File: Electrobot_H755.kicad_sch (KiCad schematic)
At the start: 107 parts, among them J1 Conn_XT30M, J10 Conn_01x04, J11 Conn_01x04, J12 Conn_01x04, J13 Conn_01x04, J14 Conn_01x04, J15 Conn_01x03, J16 Conn_01x03, J17 Conn_01x04, J18 Conn_01x03, J19 Conn_01x03, J2 Conn_01x04, J20 Conn_01x03, J21 Conn_01x03, J22 Conn_01x04, J23 Conn_01x03, J24 Conn_01x03, J25 Conn_01x03, J26 Conn_01x03, J27 Conn_01x02, J28 Conn_01x02, J29 Conn_01x02, J3 Conn_01x04, J30 Conn_01x02, J31 Conn_01x03, J32 Conn_01x03, J33 Conn_01x06, J34 Conn_01x06, J35 Conn_01x04, J36 Conn_01x02, J4 Conn_01x04, J5 Conn_01x04, J6 Conn_01x04, J7 Conn_01x04, J8 Conn_01x04, J9 Conn_01x04, U2 TSR_2-2450, U3 TSR_2-2465, U4 TSR_2-2465

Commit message: Correction empreinte condensateur
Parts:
- C4: footprint Capacitor_THT:C_Radial_D8.0mm_H11.5mm_P3.50mm -> Passive:C_Radial_D8.0mm_H11.5mm_P3.50mm
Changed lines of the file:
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@@
 			)
 		)
-		(property "Footprint" "Capacitor_THT:C_Radial_D8.0mm_H11.5mm_P3.50mm"
+		(property "Footprint" "Passive:C_Radial_D8.0mm_H11.5mm_P3.50mm"
 			(at 31.4452 27.94 0)
 			(effects

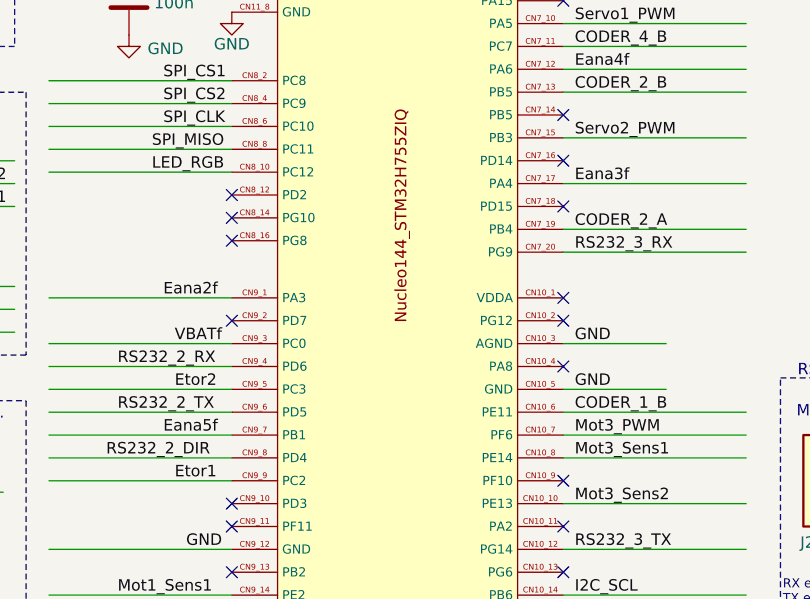
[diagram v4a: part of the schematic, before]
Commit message: Inversion Eana5f et Eana3f pour faciliter le routage
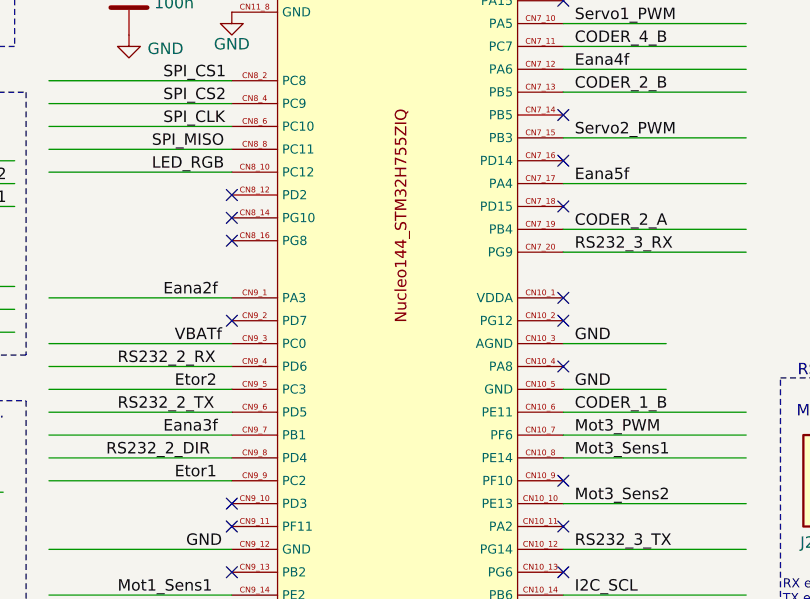
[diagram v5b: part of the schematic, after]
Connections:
- net Eana3f: now also U1.CN9_7 (PB1); no longer U1.CN7_17 (PA4)
- net Eana5f: now also U1.CN7_17 (PA4); no longer U1.CN9_7 (PB1)
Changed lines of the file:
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@@
 		)
 	)
-	(label "Eana3f"
+	(label "Eana5f"
 		(at 120.65 88.9 0)
 		(fields_autoplaced yes)
@@
 		)
 	)
-	(label "Eana5f"
+	(label "Eana3f"
 		(at 74.93 116.84 0)
 		(fields_autoplaced yes)

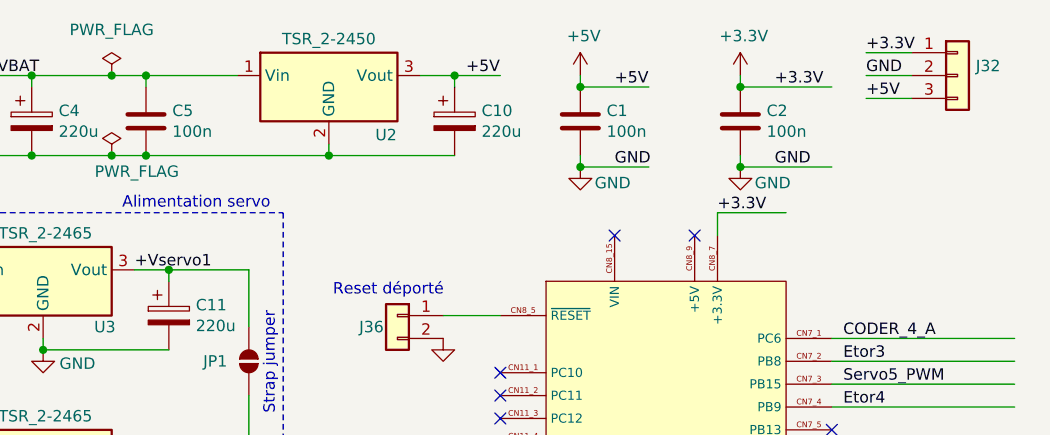
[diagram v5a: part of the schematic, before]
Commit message: Ajout des références commerciales RS et Farnell pour certains composants
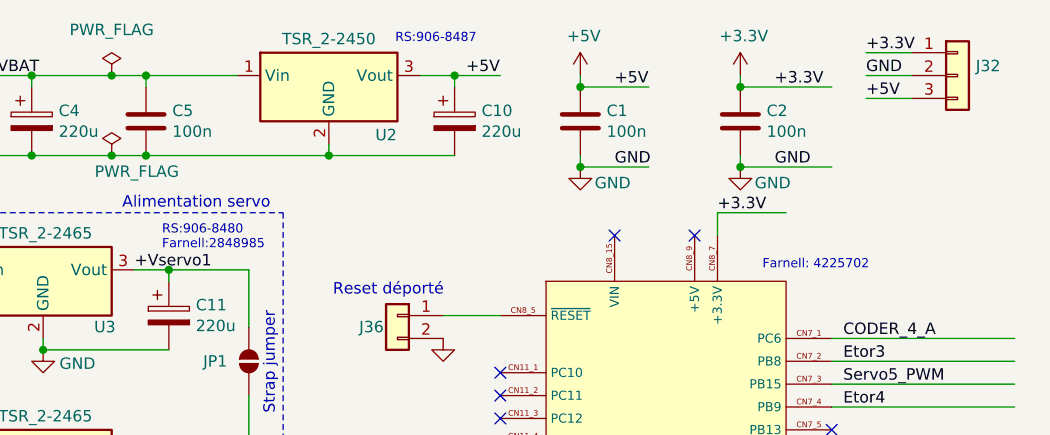
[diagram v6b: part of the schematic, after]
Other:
- note added: "Farnell: 4225702"
- note added: "RS:906-8480 Farnell:2848985"
- note added: "RS:906-8487"
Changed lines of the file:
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@@
+		)
+	)
+	(text "Farnell: 4225702"
+		(exclude_from_sim no)
+		(at 117.602 40.132 0)
+		(effects
+			(font
+				(size 1.016 1.016)
+				(color 255 123 22 1)
+			)
+		)
+	)
+	(text "RS:906-8487"
+		(exclude_from_sim no)
+		(at 70.866 14.986 0)
+		(effects
+			(font
+				(size 1.016 1.016)
+				(color 255 123 22 1)
+			)
+			(justify left)
+		)
+	)
+	(text "RS:906-8480\nFarnell:2848985"
+		(exclude_from_sim no)
+		(at 44.958 37.084 0)
+		(effects
+			(font
+				(size 1.016 1.016)
+				(color 255 123 22 1)
+			)
+			(justify left)
 		)
 	)

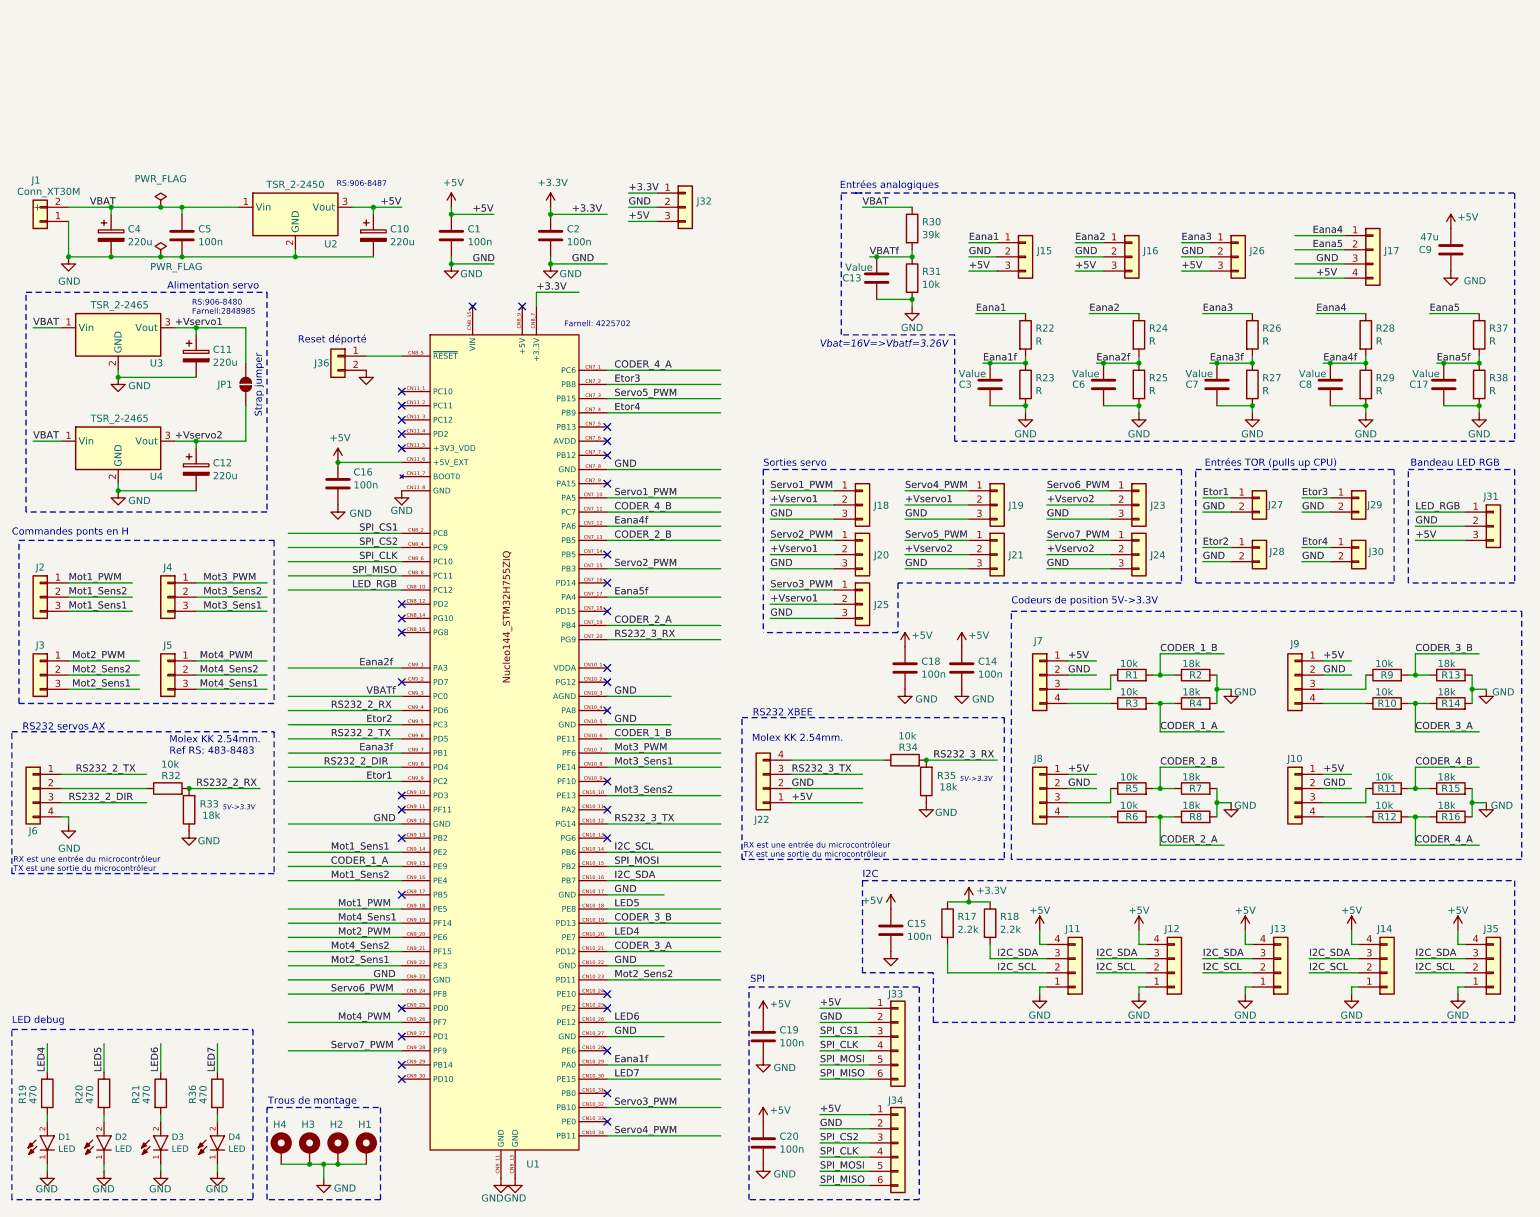
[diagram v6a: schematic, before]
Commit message: Mise à jour du schéma
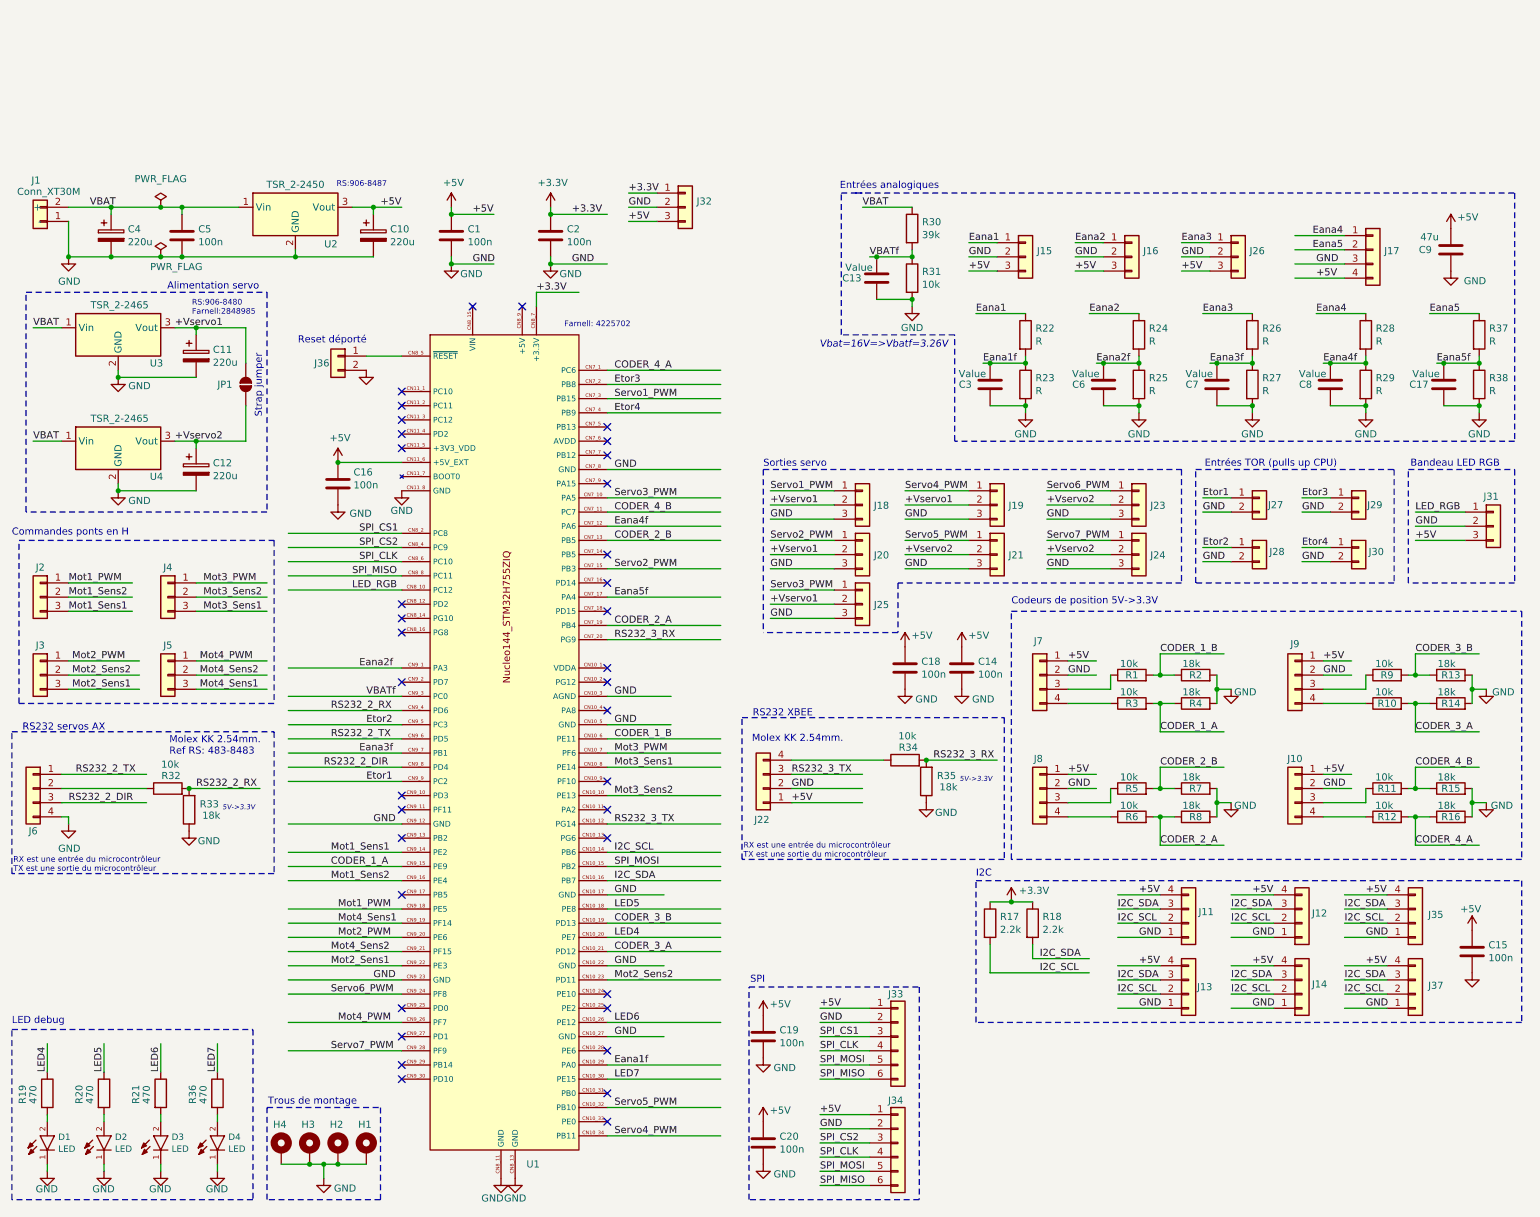
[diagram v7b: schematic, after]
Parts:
- added J37: Conn_01x04, Connector_Molex:Molex_KK-254_AE-6410-04A_1x04_P2.54mm_Vertical, symbol CRLG-Connectors:Conn_01x04
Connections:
- net +5V: now also J37.4 (Pin_4)
- net GND: now also J37.1 (Pin_1)
- net I2C_SCL: now also J37.2 (Pin_2)
- net I2C_SDA: now also J37.3 (Pin_3)
- net Servo1_PWM: now also U1.CN7_3 (PB15); no longer U1.CN7_10 (PA5)
- net Servo3_PWM: now also U1.CN7_10 (PA5); no longer U1.CN10_32 (PB10)
- net Servo5_PWM: now also U1.CN10_32 (PB10); no longer U1.CN7_3 (PB15)
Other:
- moved on the sheet: C15, J11, J12, J13, J14, J35, R17, R18

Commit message: Correction des valeurs de résistances pour les UART servos AX et XBEE
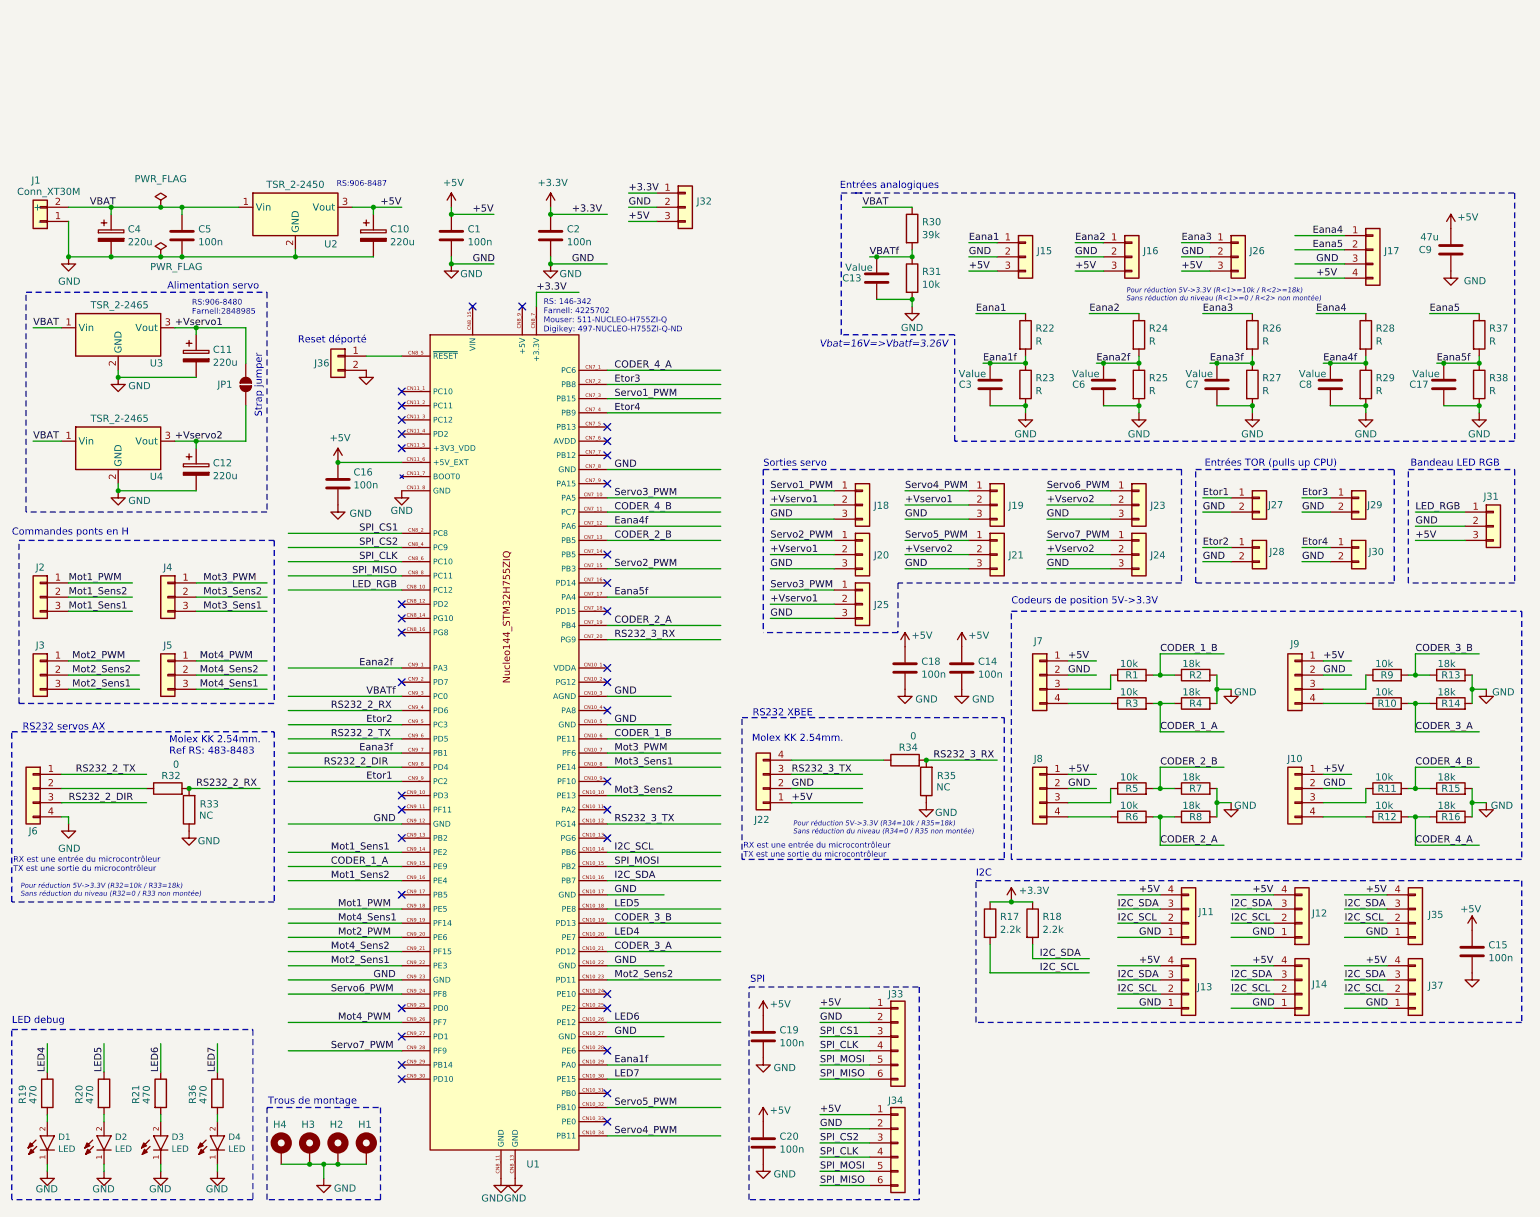
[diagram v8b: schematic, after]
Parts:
- R32, R34: value 10k -> 0
- R33, R35: value 18k -> NC
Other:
- note added: "Pour réduction 5V->3.3V (R32=10k / R33=18k) Sans réduction du niveau (R32=0 / R33 non montée)"
- note added: "Pour réduction 5V->3.3V (R34=10k / R35=18k) Sans réduction du niveau (R34=0 / R35 non montée)"
- note added: "Pour réduction 5V->3.3V (R<1>=10k / R<2>=18k) Sans réduction du niveau (R<1>=0 / R<2> non montée)"
- note added: "RS: 146-342 Farnell: 4225702 Mouser: 511-NUCLEO-H755ZI-Q Digikey: 497-NUCLEO-H755ZI-Q-ND"
- note removed: "5V->3.3V"
- note removed: "Farnell: 4225702"
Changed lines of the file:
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@@
 	(rectangle
 		(start 12.7 113.03)
-		(end 59.69 138.43)
+		(end 59.69 143.51)
 		(stroke
 			(width 0)
@@
 		)
 	)
-	(text "5V->3.3V"
-		(exclude_from_sim no)
-		(at 185.42 121.666 0)
-		(effects
-			(font
-				(size 0.889 0.889)
-				(italic yes)
-			)
-		)
-	)
 	(text "Vbat=16V=>Vbatf=3.26V"
 		(exclude_from_sim no)
@@
 		)
 	)
-	(text "5V->3.3V"
+	(text "Pour réduction 5V->3.3V (R34=10k / R35=18k)\nSans réduction du niveau (R34=0 / R35 non montée)\n\n"
+		(exclude_from_sim no)
+		(at 152.654 131.064 0)
+		(effects
+			(font
+				(size 0.889 0.889)
+				(italic yes)
+			)
+			(justify left)
+		)
+	)
+	(text "Pour réduction 5V->3.3V (R32=10k / R33=18k)\nSans réduction du niveau (R32=0 / R33 non montée)\n\n"
 		(exclude_from_sim no)
-		(at 53.34 126.746 0)
+		(at 14.224 142.24 0)
 		(effects
 			(font
@@
 				(italic yes)
 			)
+			(justify left)
 		)
 	)
@@
 		)
 	)
-	(text "Farnell: 4225702"
+	(text "RS: 146-342\nFarnell: 4225702\nMouser: 511-NUCLEO-H755ZI-Q\nDigikey: 497-NUCLEO-H755ZI-Q-ND"
 		(exclude_from_sim no)
-		(at 117.602 40.132 0)
+		(at 107.95 38.608 0)
 		(effects
 			(font
@@
 				(color 255 123 22 1)
 			)
+			(justify left)
 		)
 	)
@@
 		)
 	)
+	(text "Pour réduction 5V->3.3V (R<1>=10k / R<2>=18k)\nSans réduction du niveau (R<1>=0 / R<2> non montée)\n\n"
+		(exclude_from_sim no)
+		(at 212.344 35.56 0)
+		(effects
+			(font
+				(size 0.889 0.889)
+				(italic yes)
+			)
+			(justify left)
+		)
+	)
 	(text "Bandeau LED RGB"
 		(exclude_from_sim no)
@@
 			)
 		)
-		(property "Value" "18k"
-			(at 50.038 128.016 0)
+		(property "Value" "NC"
+			(at 48.768 128.016 0)
 			(effects
 				(font
@@
 			)
 		)
-		(property "Value" "10k"
+		(property "Value" "0"
 			(at 174.752 113.792 90)
 			(effects
@@
 			)
 		)
-		(property "Value" "10k"
+		(property "Value" "0"
 			(at 42.672 118.872 90)
 			(effects
@@
 			)
 		)
-		(property "Value" "18k"
-			(at 182.118 122.936 0)
+		(property "Value" "NC"
+			(at 180.848 122.936 0)
 			(effects
 				(font
